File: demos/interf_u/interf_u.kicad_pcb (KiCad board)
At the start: 2 copper layers, 115.6 x 108 mm, 25 parts, among them P1 DB25FEMELLE, U1 74LS245, U2 74LS688, U3 74LS541, U5 628128, U8 EP600, U9 4003APG120, X1 8MHz

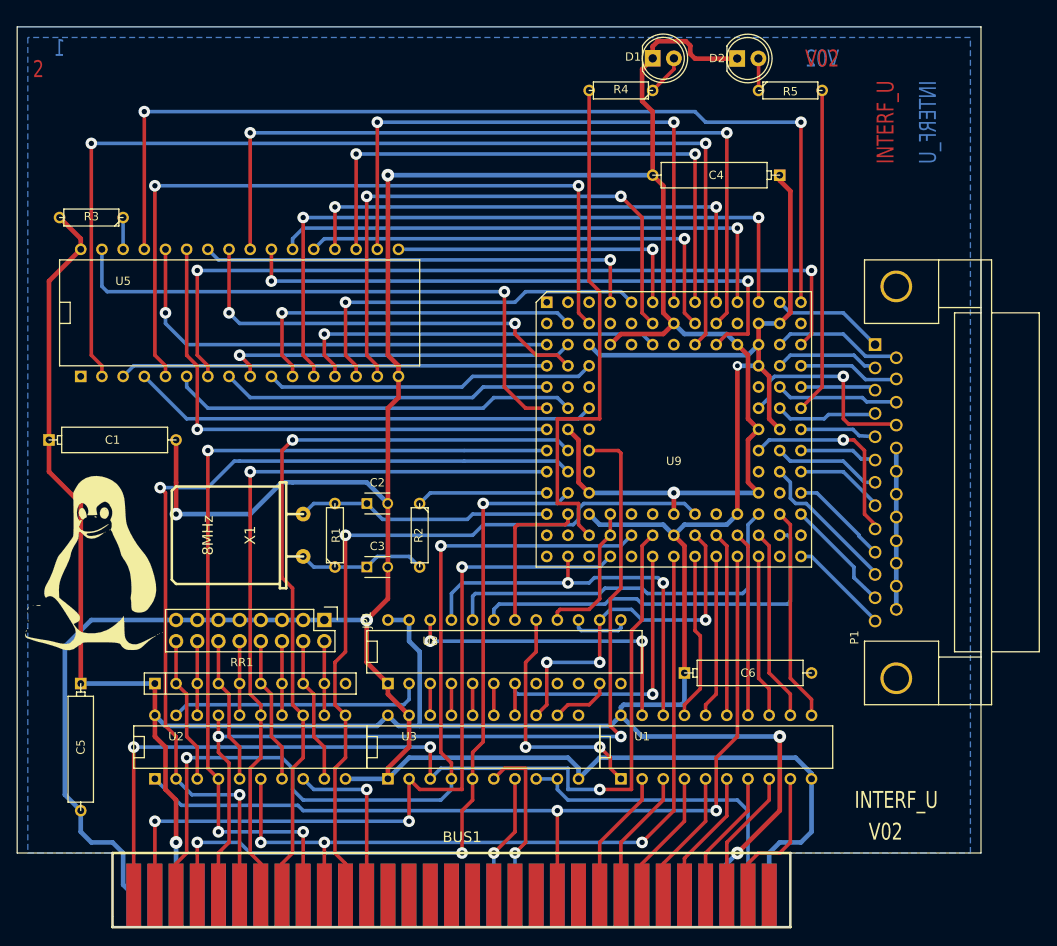
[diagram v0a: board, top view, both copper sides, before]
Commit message: Update interf_u demo to use latest libraries and the new sym-lib-table
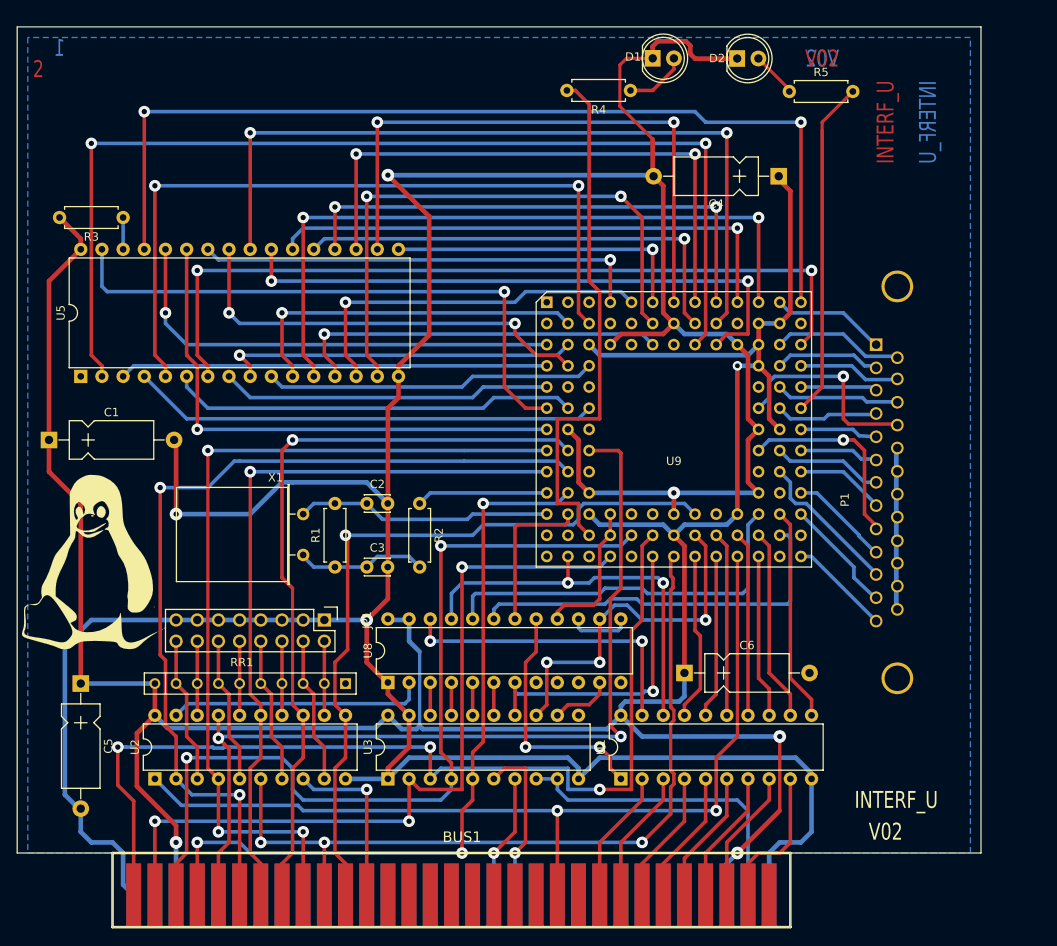
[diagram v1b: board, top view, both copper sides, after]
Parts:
- removed G***: LOGO, LOGO
- added G1: Tux, LOGO, F.Cu at (88.6, 98.4)
- C1, C4, C5, C6: footprint Discret:CP6 -> Capacitors_THT:CP_Axial_L10.0mm_D4.5mm_P15.00mm_Horizontal
- C2, C3: footprint Capacitors_ThroughHole:C_Disc_D3_P2.5 -> Capacitors_THT:C_Disc_D3.0mm_W2.0mm_P2.50mm
- P1: footprint Connect:DB25FC -> Connectors:DB25FC
- R1, R2, R3, R4, R5: footprint Discret:R3 -> Resistors_THT:R_Axial_DIN0207_L6.3mm_D2.5mm_P7.62mm_Horizontal
- U1, U2, U3: footprint Sockets_DIP:DIP-20__300 -> Housings_DIP:DIP-20_W7.62mm
- U5: footprint Sockets_DIP:DIP-32__600 -> Housings_DIP:DIP-32_W15.24mm
- U8: footprint Sockets_DIP:DIP-24__300 -> Housings_DIP:DIP-24_W7.62mm
- X1: footprint HC-18UH -> Crystals:Crystal_HC18-U_Horizontal
- moved U5 20.5 mm to (87.0, 76.2), turned to 90 degrees
- moved P1 16.5 mm to (182.4, 72.4)
- moved U8 14.4 mm to (123.8, 112.9), turned to 90 degrees
- moved U1 12.0 mm to (151.8, 124.5), turned to 90 degrees
- moved U2 12.0 mm to (95.9, 124.5), turned to 90 degrees
- moved U3 12.0 mm to (123.8, 124.5), turned to 90 degrees
- moved C1 7.62 mm to (83.2, 83.8)
- moved C5 7.62 mm to (87.0, 113.0)
- moved C6 7.62 mm to (159.4, 111.8)
- moved C4 7.49 mm to (170.7, 52.2)
- moved R1 3.81 mm to (117.5, 99.1)
- moved R2 3.81 mm to (127.6, 91.4)
- moved R3 3.81 mm to (92.1, 57.1)
- moved X1 2.54 mm to (113.7, 92.7)
- moved R4 1.14 mm to (152.9, 41.9)
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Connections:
- U8 pad 10: Net-(U8-Pad10) -> (no net)
- U8 pad 8: Net-(U8-Pad8) -> (no net)
- U8 pad 9: Net-(U8-Pad9) -> (no net)
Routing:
- net GND: track 432.6 -> 439.8 mm
- net /PC-A0: track 115.9 -> 118.7 mm
- net Net-(D1-Pad2): track 4.86 -> 7.53 mm
- net VCC: track 337.0 -> 339.4 mm
- net /LED1: track 62.0 -> 63.7 mm
- net Net-(D2-Pad2): track 3.81 -> 5.49 mm
- net /LED2: track 39.2 -> 40.6 mm
- net /PC-A9: track 95.6 -> 96.4 mm
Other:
- net class Default: trace_width 0.4318 -> 0.4; via_dia 1.397 -> 1.4
- net class Power: trace_width 0.5588 -> 0.5; via_dia 1.524 -> 1.6
- rule trace_min: 0.2032 -> 0.2

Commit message: Update demos
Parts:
- BUS1: footprint BUS_PC -> interf_u:BUS_PC
- C1, C4, C5, C6: footprint Capacitors_THT:CP_Axial_L10.0mm_D4.5mm_P15.00mm_Horizontal -> Capacitor_THT:CP_Axial_L10.0mm_D4.5mm_P15.00mm_Horizontal
- C2, C3: footprint Capacitors_THT:C_Disc_D3.0mm_W2.0mm_P2.50mm -> Capacitor_THT:C_Disc_D3.0mm_W2.0mm_P2.50mm
- D1, D2: footprint LEDs:LED-5MM -> LED_THT:LED_D5.0mm
- P1: footprint Connectors:DB25FC -> Connector_Dsub:DSUB-25_Female_Horizontal_P2.77x2.84mm_EdgePinOffset9.90mm_Housed_MountingHolesOffset11.32mm
- R4, R5: footprint Resistors_THT:R_Axial_DIN0207_L6.3mm_D2.5mm_P7.62mm_Horizontal -> Resistor_THT:R_Axial_DIN0207_L6.3mm_D2.5mm_P7.62mm_Horizontal
- RR1: footprint Discret:r_pack9 -> Resistor_THT:R_Array_SIP10
- U1, U2, U3: footprint Housings_DIP:DIP-20_W7.62mm -> Package_DIP:DIP-20_W7.62mm
- U5: footprint Housings_DIP:DIP-32_W15.24mm -> Package_DIP:DIP-32_W15.24mm
- U8: footprint Housings_DIP:DIP-24_W7.62mm -> Package_DIP:DIP-24_W7.62mm
- U9: footprint Sockets:PGA120 -> interf_u:PGA120
- X1: footprint Crystals:Crystal_HC18-U_Horizontal -> Crystal:Crystal_HC18-U_Horizontal
- moved RR1 11.4 mm to (95.9, 113.0)
- moved R4 1.14 mm to (151.8, 41.9)
- moved P1 0.27 mm to (182.1, 72.4), turned to 90 degrees
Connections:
- U8 pad 10: (no net) -> Net-(U8-Pad10)
- U8 pad 8: (no net) -> Net-(U8-Pad8)
- U8 pad 9: (no net) -> Net-(U8-Pad9)
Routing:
- net Net-(D1-Pad2): track 7.53 -> 8.67 mm
- net /LED1: track 63.7 -> 64.9 mm
- net GND: track 439.8 -> 440.8 mm
- net /BIT7: track 23.7 -> 24.7 mm

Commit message: Update demos
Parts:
- R1, R2, R3: footprint Resistors_THT:R_Axial_DIN0207_L6.3mm_D2.5mm_P7.62mm_Horizontal -> Resistor_THT:R_Axial_DIN0207_L6.3mm_D2.5mm_P7.62mm_Horizontal

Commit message: Update demos.
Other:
- net class Default: via_drill 0.635 -> 0.6
- net class Power: via_drill 0.635 -> 0.6
- rule via_min_drill: 0.508 -> 0.5
- rule via_min_size: 0.889 -> 0.9

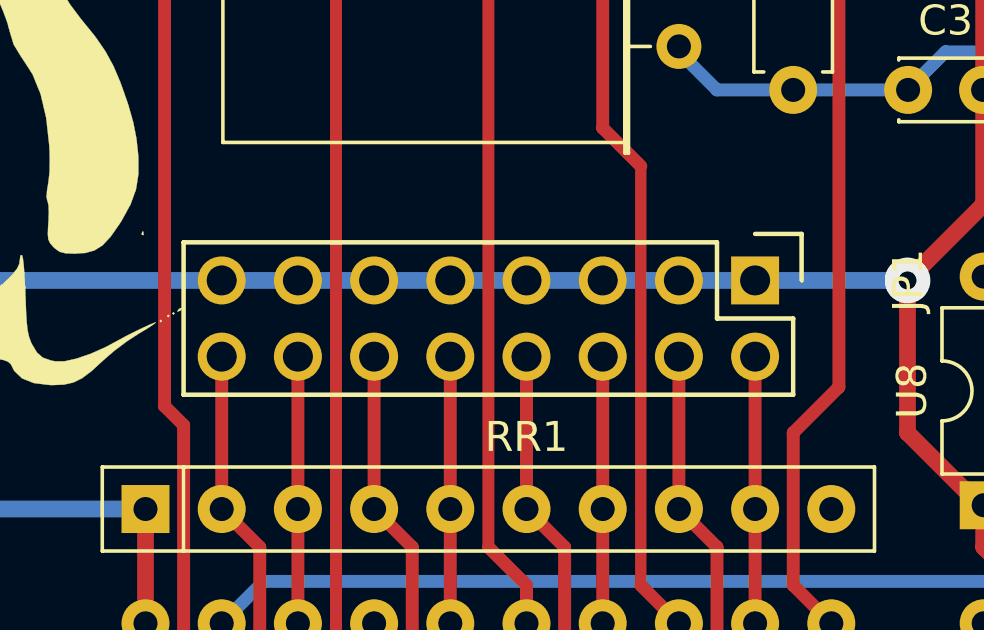
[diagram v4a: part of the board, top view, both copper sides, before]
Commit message: Update demos to use recent footprints.
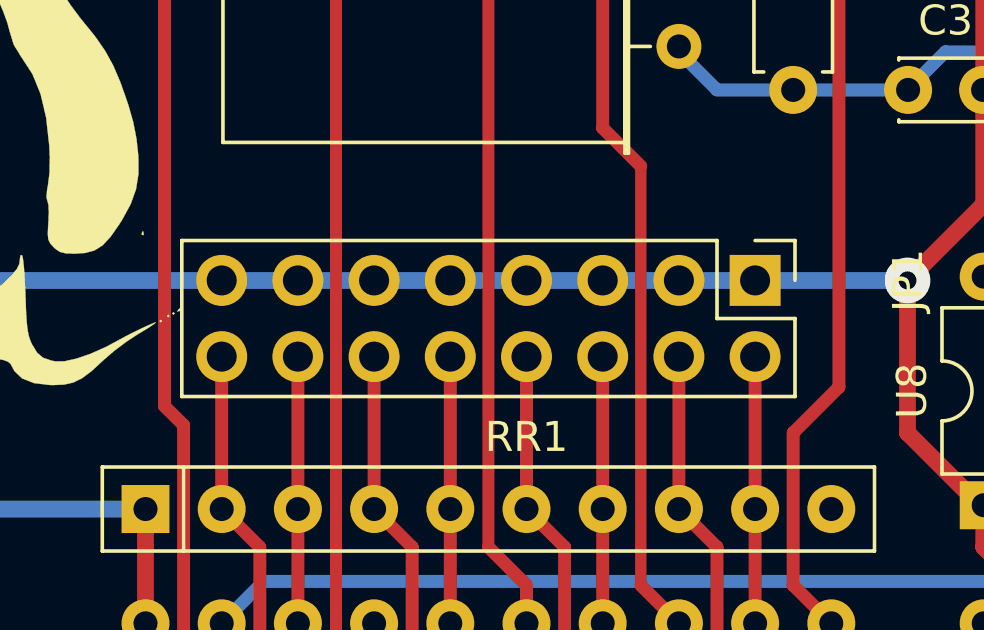
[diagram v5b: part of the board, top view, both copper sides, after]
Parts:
- JP1: footprint Pin_Headers:Pin_Header_Straight_2x08 -> Connector_PinHeader_2.54mm:PinHeader_2x08_P2.54mm_Vertical

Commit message: Update demo
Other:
- rule pad_to_mask_clearance: 0.254 -> 0.05
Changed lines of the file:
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@@
-(kicad_pcb (version 20191123) (host pcbnew "(5.99.0-593-g496f3d49e-dirty)")
+(kicad_pcb (version 20200518) (host pcbnew "(5.99.0-1885-g8575afd7e-dirty)")
   (general
     (thickness 1.6002)
@@
     (nets 174)
   )
-  (page "A4")
+  (paper "A4")
   (title_block
     (title "Demo")
@@
     (zone_45_only no)
     (trace_min 0.2)
+    (clearance_min 0.2)
+    (via_min_annulus 0.05)
+    (via_min_size 0.9)
+    (through_hole_min 0.5)
+    (hole_to_hole_min 0.25)
     (via_size 1.4)
     (via_drill 0.6)
-    (via_min_size 0.9)
-    (via_min_drill 0.5)
     (user_via 1.524 0.762)
     (uvia_size 0.5)
@@
     (uvia_min_size 0.5)
     (uvia_min_drill 0.127)
-    (max_error 0.005)
+    (max_error 0.01)
+    (filled_areas_thickness no)
     (defaults
-      (edge_clearance 0.01)
+      (edge_clearance 0)
       (edge_cuts_line_width 0.127)
       (courtyard_line_width 0.05)
@@
       (silk_line_width 0.381)
       (silk_text_dims (size 1.524 1.524) (thickness 0.3048))
+      (fab_layers_line_width 0.1)
+      (fab_layers_text_dims (size 1 1) (thickness 0.15))
       (other_layers_line_width 0.1)
       (other_layers_text_dims (size 1 1) (thickness 0.15))
@@
     (pad_size 1.397 1.397)
     (pad_drill 0.89916)
-    (pad_to_mask_clearance 0.254)
-    (solder_mask_min_width 0.5)
+    (pad_to_mask_clearance 0.05)
     (aux_axis_origin 74.93 140.97)
     (visible_elements 7FFFFF7F)
     (pcbplotparams
-      (layerselection 0x000f0_ffffffff)
+      (layerselection 0x010f0_ffffffff)
       (usegerberextensions false)
       (usegerberattributes true)
       (usegerberadvancedattributes true)
       (creategerberjobfile true)
-      (excludeedgelayer false)
-      (linewidth 0.150000)
+      (svguseinch false)
+      (svgprecision 6)
+      (excludeedgelayer true)
+      (linewidth 0.100000)
       (plotframeref false)
       (viasonmask false)
@@
       (plotvalue true)
       (plotinvisibletext false)
-      (padsonsilk false)
+      (sketchpadsonfab false)
       (subtractmaskfromsilk false)
       (outputformat 1)
@@
     (fp_line (start 4.35 19.55) (end 4.35 -1.8) (layer "F.CrtYd") (width 0.05))
     (fp_line (start 4.35 -1.8) (end -1.8 -1.8) (layer "F.CrtYd") (width 0.05))
-    (fp_text user "%R" (at 1.27 8.89) (layer "F.Fab")
+    (fp_text user "${REFERENCE}" (at 1.27 8.89) (layer "F.Fab")
       (effects (font (size 1 1) (thickness 0.15)))
     )
@@
       (effects (font (size 1 1) (thickness 0.15)))
     )
-    (fp_text user "%R" (at 3.81 0 90) (layer "F.Fab")
+    (fp_text user "${REFERENCE}" (at 3.81 0 90) (layer "F.Fab")
       (effects (font (size 1 1) (thickness 0.15)))
     )
@@
       (effects (font (size 1 1) (thickness 0.15)))
     )
-    (fp_text user "%R" (at 3.81 0 -90) (layer "F.Fab")
+    (fp_text user "${REFERENCE}" (at 3.81 0 -90) (layer "F.Fab")
       (effects (font (size 1 1) (thickness 0.15)))
     )
@@
       (effects (font (size 1 1) (thickness 0.15)))
     )
-    (fp_text user "%R" (at 3.81 0 180) (layer "F.Fab")
+    (fp_text user "${REFERENCE}" (at 3.81 0 180) (layer "F.Fab")
       (effects (font (size 1 1) (thickness 0.15)))
     )
@@
       (effects (font (size 1 1) (thickness 0.15)))
     )
-    (fp_text user "%R" (at 3.81 0 180) (layer "F.Fab")
+    (fp_text user "${REFERENCE}" (at 3.81 0 180) (layer "F.Fab")
       (effects (font (size 1 1) (thickness 0.15)))
     )
@@
       (effects (font (size 1 1) (thickness 0.15)))
     )
-    (fp_text user "%R" (at 3.81 0) (layer "F.Fab")
+    (fp_text user "${REFERENCE}" (at 3.81 0) (layer "F.Fab")
       (effects (font (size 1 1) (thickness 0.15)))
     )
@@
     (fp_line (start -1.29 1.25) (end 24.15 1.25) (layer "F.Fab") (width 0.1))
     (fp_line (start -1.29 -1.25) (end -1.29 1.25) (layer "F.Fab") (width 0.1))
-    (fp_text user "%R" (at 11.43 0) (layer "F.Fab")
+    (fp_text user "${REFERENCE}" (at 11.43 0) (layer "F.Fab")
       (effects (font (size 1 1) (thickness 0.15)))
     )
@@
       (effects (font (size 1 1) (thickness 0.15)))
     )
-    (fp_text user "%R" (at -16.62 16.225 90) (layer "F.Fab")
+    (fp_text user "${REFERENCE}" (at -16.62 16.225 90) (layer "F.Fab")
       (effects (font (size 1 1) (thickness 0.15)))
     )
@@
     (fp_line (start 4.5 3.25) (end 4.5 -3.25) (layer "F.CrtYd") (width 0.05))
     (fp_line (start 4.5 -3.25) (end -1.95 -3.25) (layer "F.CrtYd") (width 0.05))
-    (fp_text user "%R" (at 1.25 0) (layer "F.Fab")
+    (fp_text user "${REFERENCE}" (at 1.25 0) (layer "F.Fab")
       (effects (font (size 0.8 0.8) (thickness 0.2)))
     )
@@
       (effects (font (size 1 1) (thickness 0.15)))
     )
-    (fp_text user "%R" (at 1.25 0) (layer "F.Fab")
+    (fp_text user "${REFERENCE}" (at 1.25 0) (layer "F.Fab")
       (effects (font (size 0.8 0.8) (thickness 0.2)))
     )
@@
       (effects (font (size 1 1) (thickness 0.15)))
     )
-    (fp_text user "%R" (at 7.5 0) (layer "F.Fab")
+    (fp_text user "${REFERENCE}" (at 7.5 0) (layer "F.Fab")
       (effects (font (size 1 1) (thickness 0.15)))
     )
@@
       (effects (font (size 1 1) (thickness 0.15)))
     )
-    (fp_text user "%R" (at 7.5 0 -90) (layer "F.Fab")
+    (fp_text user "${REFERENCE}" (at 7.5 0 -90) (layer "F.Fab")
       (effects (font (size 1 1) (thickness 0.15)))
     )
@@
       (effects (font (size 1 1) (thickness 0.15)))
     )
-    (fp_text user "%R" (at 7.5 0 180) (layer "F.Fab")
+    (fp_text user "${REFERENCE}" (at 7.5 0 180) (layer "F.Fab")
       (effects (font (size 1 1) (thickness 0.15)))
     )
@@
       (effects (font (size 1 1) (thickness 0.15)))
     )
-    (fp_text user "%R" (at 7.5 0) (layer "F.Fab")
+    (fp_text user "${REFERENCE}" (at 7.5 0) (layer "F.Fab")
       (effects (font (size 1 1) (thickness 0.15)))
     )
@@
       (effects (font (size 1 1) (thickness 0.15)))
     )
-    (fp_text user "%R" (at 1.25 0) (layer "F.Fab")
+    (fp_text user "${REFERENCE}" (at 1.25 0) (layer "F.Fab")
       (effects (font (size 1 1) (thickness 0.15)))
     )
@@
       (effects (font (size 1 1) (thickness 0.15)))
     )
-    (fp_text user "%R" (at 1.25 0) (layer "F.Fab")
+    (fp_text user "${REFERENCE}" (at 1.25 0) (layer "F.Fab")
       (effects (font (size 1 1) (thickness 0.15)))
     )
@@
   (zone (net 100) (net_name "GND") (layer "bottom_copper") (hatch edge 0.508)
     (connect_pads (clearance 0.508))
-    (min_thickness 0.254)
+    (min_thickness 0.254) (filled_areas_thickness no)
     (fill yes (thermal_gap 0.508) (thermal_bridge_width 0.508))
     (polygon

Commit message: Update demos
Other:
- board size 115.6 x 108 mm -> 115.6 x 108.2 mm
- net class Default removed
- net class Power removed
